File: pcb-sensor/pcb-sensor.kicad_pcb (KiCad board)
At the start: 2 copper layers, 86 x 86 mm, 30 parts, among them J1 Conn_02x06_Counter_Clockwise, J2 Conn_01x03, J4 Conn_01x05, J5 Conn_01x02, J6 Conn_01x01, J7 Conn_01x01, J8 Conn_01x01, J9 Conn_01x02_Male, U1 LM340MP, U2 SFH617A-2X009T, U4 SFH617A-2X009T

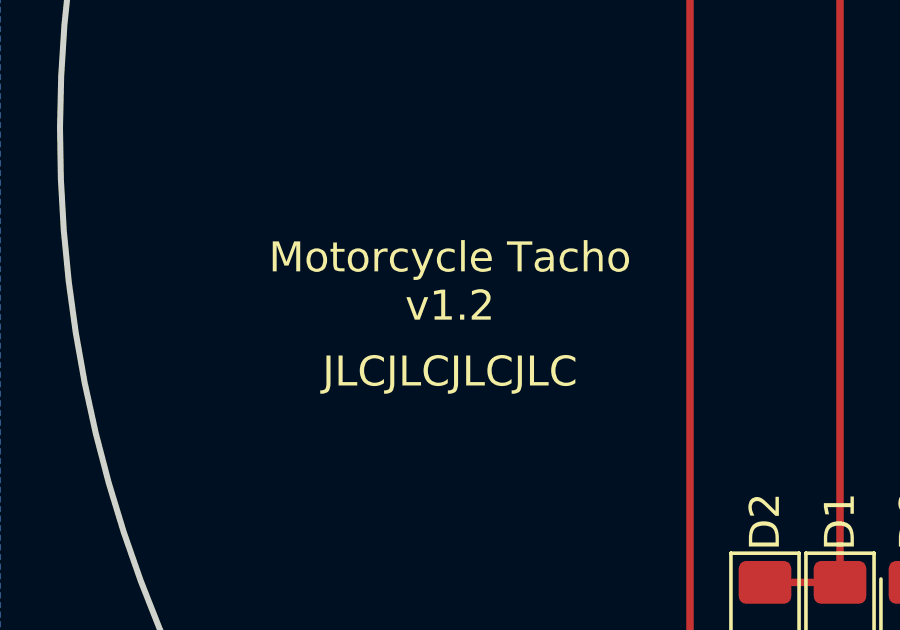
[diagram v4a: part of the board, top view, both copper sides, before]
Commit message: resolves #52: crystal circuit
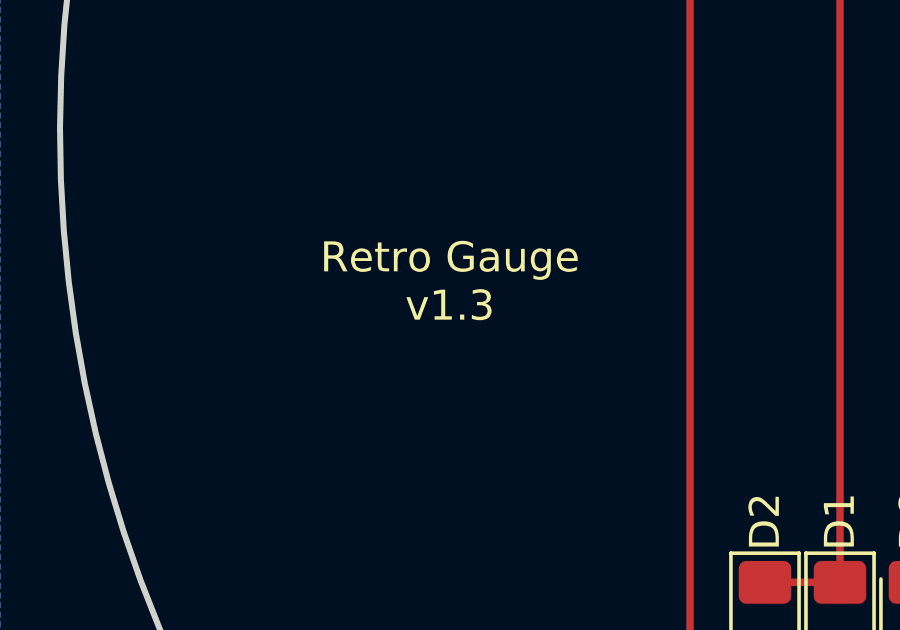
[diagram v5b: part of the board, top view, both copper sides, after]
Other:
- board text added: "Retro Gauge v1.3"
- board text removed: "JLCJLCJLCJLC"
- board text removed: "Motorcycle Tacho v1.2"
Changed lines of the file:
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@@
     (effects (font (size 1 1) (thickness 0.15)) (justify left))
   )
-  (gr_text "Motorcycle Tacho\nv1.2" (at 120 105) (layer "F.SilkS")
+  (gr_text "Retro Gauge\nv1.3" (at 120 105) (layer "F.SilkS")
     (effects (font (size 1 1) (thickness 0.15)))
   )
@@
     (effects (font (size 1 1) (thickness 0.15)) (justify right))
   )
-  (gr_text "JLCJLCJLCJLC" (at 120 108) (layer "F.SilkS")
-    (effects (font (size 1 1) (thickness 0.15)))
-  )
   (gr_text "PD5" (at 164.5 69) (layer "F.SilkS")

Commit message: update layout
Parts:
- removed J7, J8: Conn_01x01, Connector_PinSocket_2.54mm:PinSocket_1x01_P2.54mm_Vertical
- removed J9: Conn_01x02_Male, Connector_JST:JST_PH_S2B-PH-K_1x02_P2.00mm_Horizontal
- added J3: Conn_01x03_Male, Connector_JST:JST_PH_S3B-PH-K_1x03_P2.00mm_Horizontal, F.Cu at (210.8, 129.8)
- added R7: 47k, Resistor_SMD:R_1206_3216Metric_Pad1.30x1.75mm_HandSolder, F.Cu at (269.5, 90.0)
- added R9: 1k, Resistor_SMD:R_1206_3216Metric_Pad1.30x1.75mm_HandSolder, F.Cu at (211.2, 125.2)
- J2: value Conn_01x03 -> Conn_01x02_Male; footprint Connector_PinSocket_2.54mm:PinSocket_1x03_P2.54mm_Vertical -> Connector_JST:JST_PH_S2B-PH-K_1x02_P2.00mm_Horizontal
- J4: value Conn_01x05 -> Conn_01x05_Male; footprint Connector_PinSocket_2.54mm:PinSocket_1x05_P2.54mm_Vertical -> Connector_JST:JST_PH_S5B-PH-K_1x05_P2.00mm_Horizontal
- J5: value Conn_01x02 -> Conn_01x02_Male; footprint Connector_PinSocket_2.54mm:PinSocket_1x02_P2.54mm_Vertical -> Connector_JST:JST_PH_S2B-PH-K_1x02_P2.00mm_Horizontal
- J6: value Conn_01x01 -> Conn_01x03_Male; footprint Connector_PinSocket_2.54mm:PinSocket_1x01_P2.54mm_Vertical -> Connector_JST:JST_PH_S3B-PH-K_1x03_P2.00mm_Horizontal
- moved J2 120.5 mm to (268.6, 97.0), turned to 0 degrees
- moved R11 89.6 mm to (244.1, 121.2)
- moved J6 88.8 mm to (241.2, 132.2)
- moved C2 68.4 mm to (226.6, 70.1)
- moved R4 42.4 mm to (128.7, 102.0), turned to 180 degrees
- moved R10 40.9 mm to (121.1, 88.5), turned to 0 degrees
- moved U2 40.0 mm to (128.4, 95.3), turned to 90 degrees
- moved U4 39.1 mm to (120.9, 95.3), turned to 90 degrees
- moved R1 39.0 mm to (121.2, 102.0), turned to 180 degrees
- moved R8 39.0 mm to (128.7, 88.5), turned to 180 degrees
- moved R2 28.5 mm to (113.7, 98.2), turned to 0 degrees
- moved R3 28.3 mm to (113.7, 93.7), turned to 0 degrees
- moved J5 25.9 mm to (178.7, 102.2), turned to 0 degrees
- moved D5 23.0 mm to (116.2, 109.0)
- moved D4 21.4 mm to (173.2, 102.2), turned to 0 degrees
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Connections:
- D6 pad 2: /PD3 -> /PD1
- J2 pad 1: /PD2 -> /ADC6
- J2 pad 2: +12V -> GND
- J4 pad 1: /HIGH_BEAM -> /NEUTRAL
- J4 pad 2: /TURN_SIGNAL_RIGHT -> /OIL_PRESSURE
- J4 pad 4: /OIL_PRESSURE -> /TURN_SIGNAL_RIGHT
- J4 pad 5: /NEUTRAL -> /HIGH_BEAM
- J5 pad 1: GND -> Net-(D4-Pad2)
- J5 pad 2: Net-(D4-Pad2) -> GND
- J6 pad 1: /PD7 -> +12V
- R3 pad 2: /PD3 -> /PD1
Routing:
- net +5V: track 92.1 -> 16.6 mm, vias 3 -> 0
- net /PD3: track 67.7 -> 0.00 mm
- net /PD2: track 60.7 -> 0.00 mm
- net /HIGH_BEAM: track 67.5 -> 14.5 mm
- net /PD6: track 62.3 -> 9.69 mm
- net Net-(D1-Pad1): track 52.4 -> 0.00 mm
- net +12V: track 45.1 -> 16.0 mm
- net /ADC7: track 41.1 -> 14.6 mm
- net /PD4: track 17.6 -> 3.00 mm
- net /PD7: track 11.8 -> 0.00 mm
- net /ADC6: track 11.7 -> 0.00 mm
- net /PB0: track 11.2 -> 0.00 mm
- net /PD5: track 14.2 -> 4.24 mm
- net Net-(D4-Pad2): track 9.08 -> 0.00 mm
- net /PD1: track 23.6 -> 16.1 mm
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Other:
- outline, holes or cut-outs redrawn
- board text added: "Speedo"
- board text added: "Tacho"
- board text removed: "12V"
- board text removed: "HIGH_BEAM"
- board text removed: "NEUTRAL"
- board text removed: "OIL_PRES"
- board text removed: "SPEED"
- board text removed: "SPEED_12V"
- board text removed: "SPEED_GND"
- board text removed: "TURN_LEFT"
- board text removed: "TURN_RIGHT"

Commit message: update pcb layouts
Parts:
- removed J2, J5: Conn_01x02_Male, Connector_JST:JST_PH_S2B-PH-K_1x02_P2.00mm_Horizontal
- removed J3, J6: Conn_01x03_Male, Connector_JST:JST_PH_S3B-PH-K_1x03_P2.00mm_Horizontal
- removed J4: Conn_01x05_Male, Connector_JST:JST_PH_S5B-PH-K_1x05_P2.00mm_Horizontal
- added J7: Conn_02x08_Top_Bottom, Connector_Molex:Molex_Mini-Fit_Jr_5566-16A_2x08_P4.20mm_Vertical, B.Cu at (164.7, 108.8)
- J1: footprint Connector_PinSocket_2.54mm:PinSocket_2x06_P2.54mm_Vertical -> Connector_PinSocket_2.00mm:PinSocket_2x06_P2.00mm_Vertical
- moved R7 111.6 mm to (158.7, 103.0)
- moved R11 98.6 mm to (147.2, 103.0), turned to 0 degrees
- moved R9 62.4 mm to (152.9, 103.0)
- moved C2 57.7 mm to (182.2, 107.0), turned to 0 degrees
- moved R3 21.7 mm to (119.3, 114.8)
- moved R2 20.3 mm to (119.3, 117.8)
- moved D5 14.7 mm to (128.0, 117.8), turned to 180 degrees
- moved D6 10.3 mm to (128.0, 114.8), turned to 180 degrees
- moved J1 7.81 mm to (164.0, 63.0)
- moved C3 7.56 mm to (174.7, 105.0)
- moved C1 7.32 mm to (188.2, 95.2)
- moved C4 7.32 mm to (174.5, 91.7)
- moved D3 7.32 mm to (182.1, 95.2)
- moved R5 7.32 mm to (182.1, 100.2)
- moved R6 7.32 mm to (188.2, 100.2)
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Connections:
- C1 pad 1: /ADC7 -> /ADC6
- D1 pad 2: /TURN_SIGNAL_LEFT -> /Left Turn
- D2 pad 2: /TURN_SIGNAL_RIGHT -> /Right Turn
- D3 pad 2: /ADC7 -> /ADC6
- D4 pad 2: Net-(D4-Pad2) -> /Power 12V
- D5 pad 1: /NEUTRAL -> /Neutral
- D5 pad 2: /PD6 -> /PD4
- D6 pad 1: /OIL_PRESSURE -> /Oil Pressure
- D6 pad 2: /PD1 -> /PD5
- J1 pad 10: /ADC7 -> /Temp Vout
- J1 pad 3: /PD3 -> /Speedo B
- J1 pad 5: /PD2 -> /Tacho B
- R10 pad 2: /PD5 -> /PD6
- R11 pad 2: /PD2 -> /Speedo B
- R2 pad 2: /PD6 -> /PD4
- R3 pad 2: /PD1 -> /PD5
- R4 pad 1: /HIGH_BEAM -> /High Beam
- R5 pad 2: /ADC7 -> /ADC6
- R6 pad 1: /ADC7 -> /ADC6
- R7 pad 2: /ADC6 -> /Temp Vout
- R8 pad 2: /PD4 -> /PD7
- R9 pad 2: /PD3 -> /Tacho B
- U2 pad 4: /PD4 -> /PD7
- U4 pad 4: /PD5 -> /PD6
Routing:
- net +5V: track 16.6 -> 164.7 mm, vias 0 -> 7
- net /PD4: track 3.00 -> 92.7 mm
- net /PD5: track 4.24 -> 83.7 mm
- net /Speedo B: track 0.00 -> 51.0 mm
- net /Tacho B: track 0.00 -> 46.9 mm
- net +12V: track 16.0 -> 59.2 mm, vias 0 -> 1
- net /ADC6: track 0.00 -> 42.1 mm
- net /PD7: track 0.00 -> 41.8 mm
- net /PD6: track 9.69 -> 48.3 mm
- net /Temp Vout: track 0.00 -> 38.6 mm
- net /PD1: track 16.1 -> 0.00 mm
- net /Neutral: track 0.00 -> 15.6 mm
- net /ADC7: track 14.6 -> 0.00 mm
- net /HIGH_BEAM: track 14.5 -> 0.00 mm
- net /Oil Pressure: track 0.00 -> 11.9 mm
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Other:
- outline, holes or cut-outs redrawn
- board text added: "High Beam"
- board text added: "Left Turn"
- board text added: "Neutral"
- board text added: "Oil Pressure"
- board text added: "Power 12V"
- board text added: "Power GND"
- board text added: "Right Turn"
- board text added: "Speedo B"
- board text added: "Speedo C"
- board text added: "Speedo E"
- board text added: "Tacho B"
- board text added: "Tacho C"
- board text added: "Tacho E"
- board text added: "Temp GND"
- board text added: "Temp Vout"
- board text removed: "Speedo"
- board text removed: "Tacho"

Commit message: v1.3 last minute changes
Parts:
- moved C2 8.01 mm to (181.9, 115.0)
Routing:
- net +12V: track 59.2 -> 61.8 mm
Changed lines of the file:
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@@
   )
   (footprint "Capacitor_THT:CP_Radial_D8.0mm_P3.80mm" (layer "F.Cu")
-    (at 182.25 107)
+    (at 181.947349 115)
     (descr "CP, Radial series, Radial, pin pitch=3.80mm, , diameter=8mm, Electrolytic Capacitor")
     (tags "CP Radial series Radial pin pitch 3.80mm  diameter 8mm Electrolytic Capacitor")
@@
     (property "Sheetname" "")
     (attr through_hole)
-    (fp_text reference "C2" (at 7.5 0) (layer "F.SilkS")
+    (fp_text reference "C2" (at 1.852651 -5.2) (layer "F.SilkS")
       (effects (font (size 1 1) (thickness 0.15)))
     )
@@
   (segment (start 132.15 101.9875) (end 132.15 99.11) (width 0.25) (layer "F.Cu") (net 9))
   (segment (start 176.25 107) (end 176.25 108.75) (width 0.5) (layer "F.Cu") (net 10))
-  (segment (start 182.25 107) (end 176.25 107) (width 0.5) (layer "F.Cu") (net 10))
+  (segment (start 181.947349 114.447349) (end 181.947349 115) (width 0.5) (layer "F.Cu") (net 10))
   (segment (start 171.25 107) (end 176.25 107) (width 0.5) (layer "F.Cu") (net 10))
   (segment (start 176.4 104.85) (end 176.4 100) (width 0.5) (layer "F.Cu") (net 10))
   (segment (start 176.25 105) (end 176.25 107) (width 0.5) (layer "F.Cu") (net 10))
   (segment (start 176.25 105) (end 176.4 104.85) (width 0.5) (layer "F.Cu") (net 10))
+  (segment (start 176.25 108.75) (end 181.947349 114.447349) (width 0.5) (layer "F.Cu") (net 10))
   (segment (start 176.4 100) (end 180.3 100) (width 0.5) (layer "F.Cu") (net 10))
   (segment (start 180.3 100) (end 180.5 100.2) (width 0.5) (layer "F.Cu") (net 10))
